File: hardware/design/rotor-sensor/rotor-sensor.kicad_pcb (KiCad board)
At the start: 2 copper layers, 42 x 34.7 mm, 88 parts, among them J2 Conn_01x06, J4 Conn_ARM_JTAG_SWD_10, U1 MCP2021A-500E/SN, U2 AP22804AW5, U4 AP2127K-ADJTRG1, U5 AP22804AW5, U6 ATSAMD21E18A-A, Y1 ABS07-32.768KHZ-7-T

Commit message: Finalizing hardware design
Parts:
- added FID1: Fiducial, Fiducial:Fiducial_0.5mm_Mask1mm, F.Cu at (123.9, 82.4)
- added FID2: Fiducial, Fiducial:Fiducial_0.5mm_Mask1mm, F.Cu at (90.4, 58.3)
- added R21: 10k, Resistor_SMD:R_0402_1005Metric, F.Cu at (98.0, 75.2)
- added R22: 10k, Resistor_SMD:R_0402_1005Metric, B.Cu at (103.2, 75.1)
- moved C14 89.5 mm to (105.5, 51.0)
- moved C24 89.5 mm to (103.2, 72.8)
- moved C9 89.5 mm to (93.0, 55.5)
- moved D2 89.5 mm to (85.4, 73.3)
- moved J2 89.5 mm to (115.1, 78.9)
- moved J4 89.5 mm to (104.0, 53.1)
- moved R1 89.5 mm to (101.9, 68.1)
- moved R20 89.5 mm to (104.3, 68.1)
- moved TP10 89.5 mm to (88.5, 75.9)
- moved TP13 89.5 mm to (85.0, 62.5)
- moved TP16 89.5 mm to (93.0, 70.0)
- moved TP19 89.5 mm to (97.6, 52.0)
- moved TP2 89.5 mm to (93.8, 76.9)
- moved TP3 89.5 mm to (123.6, 76.9)
- moved TP6 89.5 mm to (98.4, 81.5)
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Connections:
- net /M04_EN1/~{SLEEP}/DIAG renamed /M04_~{SLEEP}/DIAG/EN1
- net /M04_INPUT1 renamed /M04_INPUT1/~{ERR}/INPUT1
- net /M04_INPUT1_DIAG renamed /M04_INPUT1_DIAG/OE/~{FLAG}
- net /M04_INPUT2 renamed /M04_INPUT2/INPUT2/INPUT2
- net /M04_INPUT2_DIAG/INPUT2 renamed /M04_INPUT2_DIAG/INPUT1/~{FLAG}
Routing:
- net +BATT: track 36.1 -> 61.8 mm
- net Net-(U2-~{FLG}): track 1.91 -> 12.6 mm
- net /M07_IN1_IN: track 30.6 -> 23.0 mm
- net GND: track 15.7 -> 21.1 mm, vias 41 -> 90
- net +5V: track 43.6 -> 48.2 mm
- net /M07_IN2_IN: track 36.8 -> 32.7 mm, vias 1 -> 2
- net Net-(U5-~{FLG}): track 1.59 -> 4.28 mm, vias 0 -> 1
- net /M07_IN2_VSUP: track 23.4 -> 25.5 mm, vias 1 -> 3
- net /M04_INPUT2/INPUT2/INPUT2: track 34.0 -> 34.9 mm
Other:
- outline, holes or cut-outs redrawn

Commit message: Fab. layer cleanup
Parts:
- U3: value ~ -> BMI088

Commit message: Hardware design finalization
FIxing architecture diagram
Changes to PCB fab layer
Fixes DNF components in schematic
Increases document width
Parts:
- R1, R7: value 10k -> 4.7k
- R18, R19, R2, R3: value 1k -> 0
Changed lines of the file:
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@@
         (effects (font (size 1 1) (thickness 0.15)))
     )
-    (fp_text value "10k" (at 0.471752 -9.121 90) (layer "F.Fab") hide
+    (fp_text value "4.7k" (at 0.471752 -9.121 90) (layer "F.Fab") hide
         (effects (font (size 1 1) (thickness 0.15)))
     )
@@
         (effects (font (size 1 1) (thickness 0.15)))
     )
-    (fp_text value "10k" (at 0 1.17 90) (layer "F.Fab") hide
+    (fp_text value "4.7k" (at 0 1.17 90) (layer "F.Fab") hide
         (effects (font (size 1 1) (thickness 0.15)))
     )
@@
         (effects (font (size 1 1) (thickness 0.15)) (justify mirror))
     )
-    (fp_text value "1k" (at 0 -1.17) (layer "B.Fab")
+    (fp_text value "0" (at 0 -1.17) (layer "B.Fab")
         (effects (font (size 1 1) (thickness 0.15)) (justify mirror))
     )
@@
         (effects (font (size 1 1) (thickness 0.15)) (justify mirror))
     )
-    (fp_text value "1k" (at 0 1.351) (layer "B.Fab")
+    (fp_text value "0" (at 0 1.351) (layer "B.Fab")
         (effects (font (size 1 1) (thickness 0.15)) (justify mirror))
     )
@@
         (effects (font (size 1 1) (thickness 0.15)) (justify mirror))
     )
-    (fp_text value "1k" (at 0 1.351) (layer "B.Fab")
+    (fp_text value "0" (at 0 1.351) (layer "B.Fab")
         (effects (font (size 1 1) (thickness 0.15)) (justify mirror))
     )
@@
         (effects (font (size 1 1) (thickness 0.15)) (justify mirror))
     )
-    (fp_text value "1k" (at 0 -1.17) (layer "B.Fab")
+    (fp_text value "0" (at 0 -1.17) (layer "B.Fab")
         (effects (font (size 1 1) (thickness 0.15)) (justify mirror))
     )

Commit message: Hardware Gen2 design freeze (#14)
* Fix label in connector schematic and added JWPF 3 pin connector
* Optical sensor adapter & CI workflow changes
* 5V rail renamed to VCC
* Fixed size information on some resistors
* Added Hall sensor position on PCB
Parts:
- R18, R19, R2, R3: value 0 -> 1k
- U1: value MCP2021A-500E/SN -> MCP2021A-xxxE/SN
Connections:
- net +5V renamed VCC

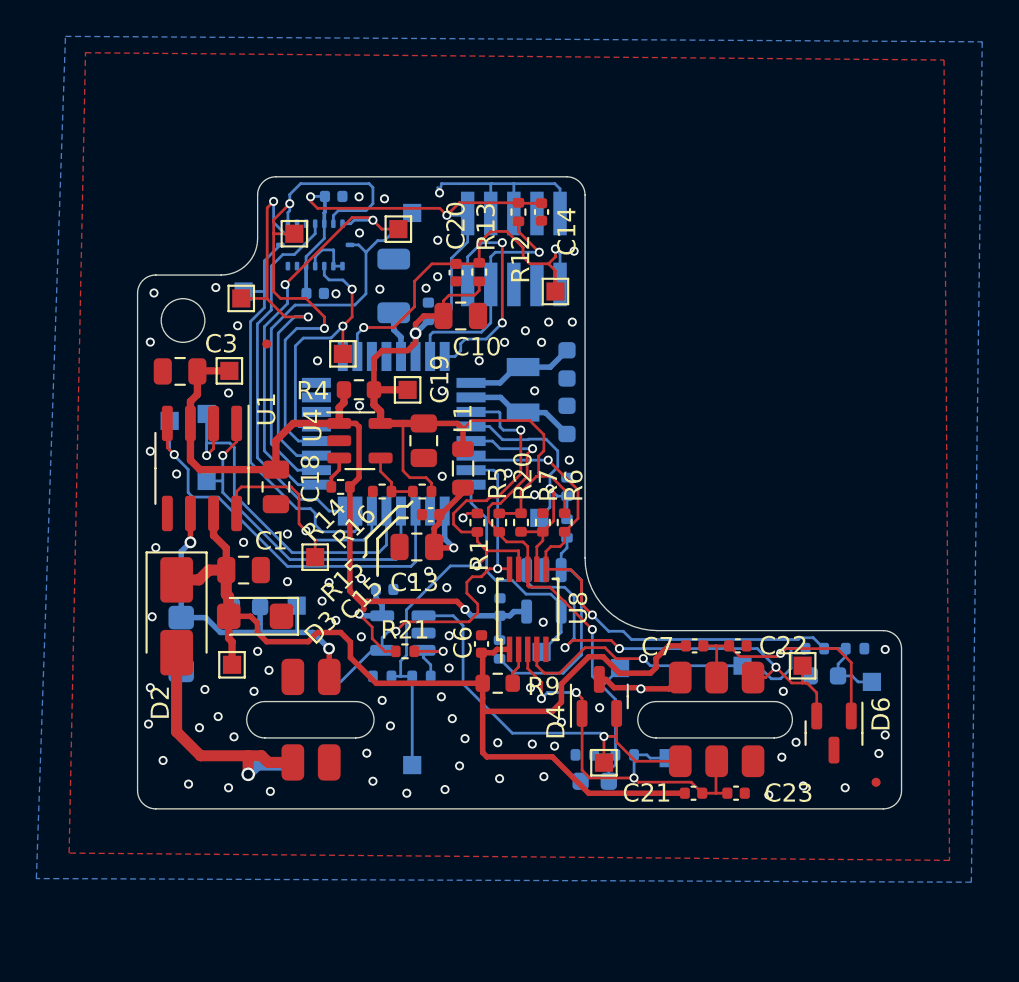
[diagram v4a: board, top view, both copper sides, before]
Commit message: Gen2.1 final hardware design (#16)
* New schematic done

Works with TLIN1028-Q1 transceiver
Added BMP581 pressure sensor
Removed 3wire output stage

* FInal ordered hardware

New 3pin connector
Extra 2pin connector for cadence measurement
No 3pin sensor variant
DC/DC converter for MCU
Pressure sensor
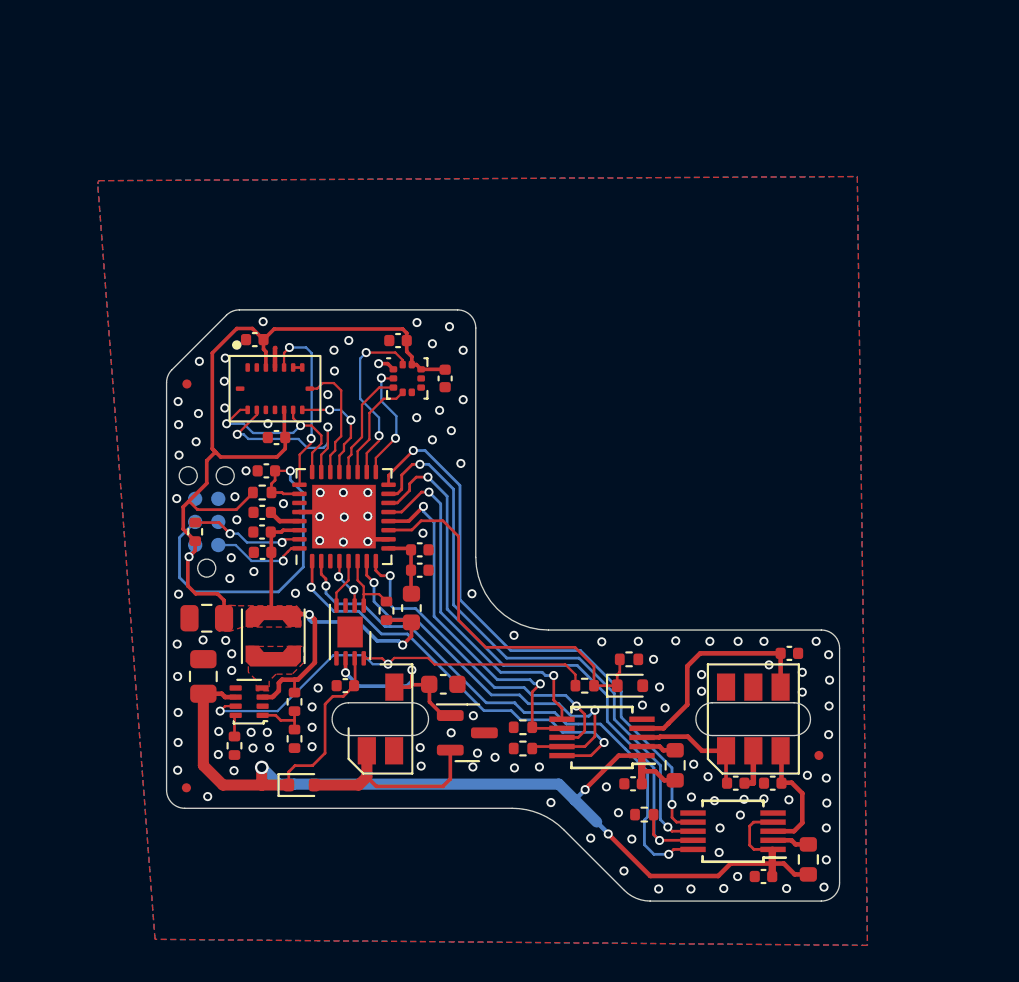
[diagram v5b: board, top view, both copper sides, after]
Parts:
- removed C13, C18, C19: 10u, Capacitor_SMD:C_0805_2012Metric
- removed C14, C21, C22, C24: 220n, Capacitor_SMD:C_0402_1005Metric
- removed C17: 1u, Capacitor_SMD:C_1206_3216Metric
- removed C25: 22n, Capacitor_SMD:C_0603_1608Metric
- removed D3: SMF33CA-DIO, Diode_SMD:D_SMF
- removed D6: PESD5V0S2BT, Package_TO_SOT_SMD:SOT-23
- removed FID2: Fiducial, Fiducial:Fiducial_0.5mm_Mask1mm
- removed J4: Conn_ARM_JTAG_SWD_10, Connector_PinHeader_1.27mm:PinHeader_2x05_P1.27mm_Vertical_SMD
- removed R10, R11, R19, R8: 1k, Resistor_SMD:R_0402_1005Metric
- removed R14, R20, R21, R22: 10k, Resistor_SMD:R_0402_1005Metric
- removed R16: 1.5k, Resistor_SMD:R_0402_1005Metric
- removed TP1: O5, TestPoint:TestPoint_Pad_1.0x1.0mm
- removed TP10: V2, TestPoint:TestPoint_Pad_1.0x1.0mm
- removed TP11: V1, TestPoint:TestPoint_Pad_1.0x1.0mm
- removed TP12: B1, TestPoint:TestPoint_Pad_1.0x1.0mm
- removed TP13: B2, TestPoint:TestPoint_Pad_1.0x1.0mm
- removed TP14: B3, TestPoint:TestPoint_Pad_1.0x1.0mm
- removed TP15: B4, TestPoint:TestPoint_Pad_1.0x1.0mm
- removed TP16: B5, TestPoint:TestPoint_Pad_1.0x1.0mm
- removed TP17: S1, TestPoint:TestPoint_Pad_1.0x1.0mm
- removed TP19: S3, TestPoint:TestPoint_Pad_1.0x1.0mm
- removed TP2: O6, TestPoint:TestPoint_Pad_1.0x1.0mm
- removed TP20: S4, TestPoint:TestPoint_Pad_1.0x1.0mm
- removed TP21: S5, TestPoint:TestPoint_Pad_1.0x1.0mm
- removed TP22: S6, TestPoint:TestPoint_Pad_1.0x1.0mm
- removed TP23: S7, TestPoint:TestPoint_Pad_1.0x1.0mm
- removed TP27: M1, TestPoint:TestPoint_Pad_1.0x1.0mm
- removed TP28: O4, TestPoint:TestPoint_Pad_1.0x1.0mm
- removed TP29: O2, TestPoint:TestPoint_Pad_1.0x1.0mm
- removed TP3: O7, TestPoint:TestPoint_Pad_1.0x1.0mm
- removed TP30: O1, TestPoint:TestPoint_Pad_1.0x1.0mm
- removed TP4: O8, TestPoint:TestPoint_Pad_1.0x1.0mm
- removed TP5: O9, TestPoint:TestPoint_Pad_1.0x1.0mm
- removed TP6: O10, TestPoint:TestPoint_Pad_1.0x1.0mm
- removed TP7: O3, TestPoint:TestPoint_Pad_1.0x1.0mm
- removed TP8: P1, TestPoint:TestPoint_Pad_1.0x1.0mm
- removed TP9: P2, TestPoint:TestPoint_Pad_1.0x1.0mm
- removed U4: AP2127K-ADJTRG1, Package_TO_SOT_SMD:SOT-23-5
- removed U5: AP22804AW5, Package_TO_SOT_SMD:SOT-23-5
- removed Y1: ABS07-32.768KHZ-7-T, Crystal:Crystal_SMD_3215-2Pin_3.2x1.5mm
- added C27: 100n, Capacitor_SMD:C_0402_1005Metric, F.Cu at (119.1, 75.3)
- added C600: 100n, Capacitor_SMD:C_0402_1005Metric, F.Cu at (97.6, 58.1)
- added C601: 100n, Capacitor_SMD:C_0402_1005Metric, F.Cu at (100.2, 60.2)
- added FID3: Fiducial, Fiducial:Fiducial_0.5mm_Mask1mm, F.Cu at (86.0, 60.5)
- added FID4: Fiducial, Fiducial:Fiducial_0.5mm_Mask1mm, F.Cu at (120.7, 80.9)
- added J1: Conn_ARM_SWD_TagConnect_TC2030-NL, Connector:Tag-Connect_TC2030-IDC-NL_2x03_P1.27mm_Vertical, B.Cu at (87.1, 68.1)
- added L3: 2.2u, Inductor_SMD:L_Coilcraft_LPS3010, F.Cu at (90.7, 74.4)
- added U10: ATSAMD21E18A-MUT, Package_DFN_QFN:VQFN-32-1EP_5x5mm_P0.5mm_EP3.5x3.5mm, F.Cu at (94.6, 67.8)
- added U600: BMP581, local_footprints:Bosch_LGA10, F.Cu at (98.1, 60.2)
- C1, C3: value 10u -> 100n; footprint Capacitor_SMD:C_0805_2012Metric -> Capacitor_SMD:C_0402_1005Metric
- C10: value 10u -> 220p; footprint Capacitor_SMD:C_0805_2012Metric -> Capacitor_SMD:C_0603_1608Metric
- C11: value 6.8p -> 22u; footprint Capacitor_SMD:C_0603_1608Metric -> Capacitor_SMD:C_0805_2012Metric; moved to F.Cu
- C12, C8, C9: value 220n -> 100n; moved to F.Cu
- C15, C20, C23, C6: value 220n -> 100n
- C16: value 6.8p -> 10u; footprint Capacitor_SMD:C_0603_1608Metric -> Capacitor_SMD:C_0805_2012Metric; moved to F.Cu
- C2: value 220p -> 100n; footprint Capacitor_SMD:C_0603_1608Metric -> Capacitor_SMD:C_0402_1005Metric; moved to F.Cu
- C4: value 22n -> 10u; footprint Capacitor_SMD:C_0603_1608Metric -> Capacitor_SMD:C_0402_1005Metric; moved to F.Cu
- C5: value 220n -> 10u; moved to F.Cu
- C7: value 220n -> 2.2u
- D1: value SMF33CA-DIO -> BAS3005B02; footprint Diode_SMD:D_SMF -> Diode_SMD:D_SOD-523; moved to F.Cu
- D2: value B140-13-F -> MM5Z3V6T1G; footprint Diode_SMD:D_SMA -> Diode_SMD:D_SOD-523
- D4: value PESD5V0S2BT -> SDT23C15L02
- J2: footprint local_footprints:SMD_6PIN -> local_footprints:SOIC-6
- L1: footprint Inductor_SMD:L_0805_2012Metric -> Inductor_SMD:L_0603_1608Metric
- R17, R3: value 1k -> 4.7k; moved to F.Cu
- R18: value 1k -> 63.4k; footprint Resistor_SMD:R_0402_1005Metric -> Resistor_SMD:R_0603_1608Metric; moved to F.Cu
- R2: value 1k -> 47k; moved to F.Cu
- R4: value 0 -> 4.7k; footprint Resistor_SMD:R_0603_1608Metric -> Resistor_SMD:R_0402_1005Metric
- R5: value 10k -> 20k
- R6: value 10k -> 4.7k
- R7: value 4.7k -> 0
- U1: value MCP2021A-xxxE/SN -> MAX9621AUB+T; footprint Package_SO:SOIC-8_3.9x4.9mm_P1.27mm -> Package_SO:MSOP-10_3x3mm_P0.5mm
- U2: value AP22804AW5 -> MCP2003BT-E/MC; footprint Package_TO_SOT_SMD:SOT-23-5 -> Package_DFN_QFN:DFN-8-1EP_3x2mm_P0.5mm_EP1.7x1.4mm; moved to F.Cu
- U3: moved to F.Cu
- U6: value ATSAMD21E18A-A -> TPS629210DRLR; footprint Package_QFP:TQFP-32_7x7mm_P0.8mm -> Package_TO_SOT_SMD:SOT-583-8; moved to F.Cu
- U7: footprint local_footprints:SMD_4PIN -> local_footprints:SOIC-4
- U8: value ~ -> MAX9621AUB+T
- moved C3 38.0 mm to (116.2, 82.4)
- moved FID1 37.9 mm to (86.0, 82.7)
- moved C4 31.6 mm to (90.1, 69.8)
- moved U1 26.5 mm to (108.8, 79.9), turned to 180 degrees
- moved C16 26.3 mm to (86.9, 76.6)
- moved D2 25.2 mm to (110.3, 77.1), turned to 0 degrees
- moved R12 25.0 mm to (86.4, 68.6), turned to 90 degrees
- moved C7 24.9 mm to (90.1, 67.6), turned to 0 degrees
- moved C1 24.4 mm to (110.5, 82.5), turned to 0 degrees
- moved C11 22.6 mm to (87.1, 73.4), turned to 180 degrees
- moved R7 20.9 mm to (88.6, 80.4)
- moved C10 20.3 mm to (100.1, 77.0), turned to 0 degrees
- moved C6 20.1 mm to (117.7, 87.6), turned to 0 degrees
- moved R9 19.6 mm to (120.1, 86.6), turned to 90 degrees
- moved R6 19.0 mm to (91.9, 80.0), turned to -90 degrees
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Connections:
- C10 pad 1: GND -> /M03_LINE
- C10 pad 2: +3.3V -> GND
- C11 pad 1: /M05_XOUT32 -> +3.3V
- C16 pad 1: /M05_XIN32 -> GND
- C16 pad 2: GND -> +BATT
- C2 pad 1: Net-(D1-A2) -> GND
- C2 pad 2: GND -> +BATT
- C23 pad 2: /M07_IN1_IN -> /M04_IN3_IN
- C3 pad 1: VCC -> GND
- C3 pad 2: GND -> /M04_IN1_IN
- C4 pad 2: /M04_INPUT2/INPUT2/INPUT2 -> +3.3V
- C5 pad 2: VCC -> /VDDANA
- C7 pad 1: /M07_IN2_IN -> GND
- C7 pad 2: +BATT -> /VDDCORE
- D1 pad 1: GND -> +BATT
- D1 pad 2: Net-(D1-A2) -> VS
- D2 pad 1: +BATT -> /M03_VMON
- D2 pad 2: Net-(D2-A) -> GND
- D4 pad 1: /M07_IN1_IN -> /M03_LINE
- D4 pad 2: /M07_IN1_VSUP -> VS
- J2 pad 1: GND -> /M04_IN1_IN
- J2 pad 2: /M07_IN2_IN -> GND
- J2 pad 3: /M07_IN2_VSUP -> /M04_IN3_IN
- J2 pad 4: /M07_IN1_VSUP -> /M04_IN2_IN
- J2 pad 5: /M07_IN1_IN -> GND
- R1 pad 2: /M04_INPUT1_DIAG/OE/~{FLAG} -> /M04_INPUT3_DIAG/OE
- R15 pad 1: Net-(U4-ADJ) -> GND
- R15 pad 2: +3.3V -> /M04_INPUT2_DIAG/INPUT1
- R17 pad 2: /M04_INPUT1_DIAG/OE/~{FLAG} -> /M04_INPUT1_DIAG/OE
- R18 pad 1: GND -> +BATT
- R18 pad 2: /M04_INPUT1/~{ERR}/INPUT1 -> Net-(U1-ISET)
- R2 pad 1: /M04_INPUT2/INPUT2/INPUT2 -> /M03_REGEN
- R2 pad 2: /M07_IN2_IN -> /M03_VMON
- R3 pad 1: GND -> /M03_VMON
- R3 pad 2: /M04_INPUT2/INPUT2/INPUT2 -> GND
- R4 pad 2: VCC -> /M03_RXD
- R5 pad 1: /M04_INPUT1/~{ERR}/INPUT1 -> +3.3V
- R5 pad 2: +3.3V -> /TPS629210_FB
- R6 pad 1: /M04_INPUT2/INPUT2/INPUT2 -> /TPS629210_FB
- R6 pad 2: +3.3V -> GND
- R7 pad 1: GND -> /TPS629210_MODE
- R7 pad 2: /M04_INPUT2_DIAG/INPUT1/~{FLAG} -> GND
- U1 pad 1: /M02_RXD -> +BATT
- U1 pad 2: /M02_CS -> Net-(U1-ISET)
- U1 pad 3: VCC -> /M04_IN1_IN
- U1 pad 4: /M02_TXD -> /M04_IN2_IN
- U1 pad 6: Net-(D1-A2) -> /M04_INPUT2/INPUT2
- U1 pad 7: +BATT -> /M04_INPUT2_DIAG/INPUT1
- U1 pad 8: /M02_TXE -> /M04_INPUT1/~{ERR}
- U2 pad 1: /M07_IN2_VSUP -> /M03_RXD
- U2 pad 2: GND -> /M03_EN
- U2 pad 3: Net-(U2-~{FLG}) -> unconnected-(U2-~{WAKE}-Pad3)
- U2 pad 4: /M04_EN2 -> /M03_TXD
- U2 pad 5: VCC -> GND
- U3 pad 10: /M06_SDO -> /M06_BMI088_MISO
- U3 pad 12: /M06_GYRO_INT -> unconnected-(U3-INT3-Pad12)
- U3 pad 14: /M06_CS_ACCEL -> /M06_BMI088_CSA
- U3 pad 15: /M06_SDO -> /M06_BMI088_MISO
- U3 pad 16: /M06_ACCEL_INT -> unconnected-(U3-INT1-Pad16)
- U3 pad 5: /M06_CS_GYRO -> /M06_BMI088_CSG
- U3 pad 8: /M06_SCK -> /M05_BMI088_SCK
- U3 pad 9: /M06_SDI -> /M05_BMI088_MOSI
- U6 pad 1: /M05_XIN32 -> /TPS629210_FB
- U6 pad 2: /M05_XOUT32 -> unconnected-(U6-PG-Pad2)
- U6 pad 3: /M04_INPUT1_DIAG/OE/~{FLAG} -> +3.3V
- U6 pad 4: /M04_INPUT2_DIAG/INPUT1/~{FLAG} -> /TPS629210_SW
- U6 pad 5: /M04_INPUT1/~{ERR}/INPUT1 -> GND
- U6 pad 6: /M04_INPUT2/INPUT2/INPUT2 -> +BATT
- U6 pad 7: /M04_~{SLEEP}/DIAG/EN1 -> /M03_REGEN
- U6 pad 8: /M04_EN2 -> /TPS629210_MODE
- U7 pad 1: Net-(D2-A) -> VS
- U7 pad 2: unconnected-(U7-Pad2) -> GND
- U7 pad 3: Net-(D1-A2) -> /M03_LINE
- U8 pad 10: /M04_~{SLEEP}/DIAG/EN1 -> /M04_~{SLEEP2}/DIAG2
- U8 pad 3: /M07_IN1_IN -> /M04_IN3_IN
- U8 pad 4: /M07_IN2_IN -> +BATT
- U8 pad 6: /M04_INPUT2/INPUT2/INPUT2 -> unconnected-(U8-DOUT2-Pad6)
- U8 pad 7: /M04_INPUT2_DIAG/INPUT1/~{FLAG} -> /M04_NC/INPUT3
- U8 pad 8: /M04_INPUT1/~{ERR}/INPUT1 -> /M04_INPUT3/~{ERR}
- U8 pad 9: /M04_INPUT1_DIAG/OE/~{FLAG} -> /M04_INPUT3_DIAG/OE
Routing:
- net VCC: track 48.2 -> 0.00 mm, vias 2 -> 0
- net /M04_INPUT2/INPUT2/INPUT2: track 34.9 -> 0.00 mm, vias 2 -> 0
- net /M04_INPUT3_DIAG/OE: track 0.00 -> 34.0 mm, vias 0 -> 2
- net /M07_IN2_IN: track 32.7 -> 0.00 mm, vias 2 -> 0
- net /M04_INPUT3/~{ERR}: track 0.00 -> 32.5 mm, vias 0 -> 2
- net /M04_INPUT1_DIAG/OE/~{FLAG}: track 32.4 -> 0.00 mm, vias 2 -> 0
- net /M04_NC/INPUT3: track 0.00 -> 32.4 mm, vias 0 -> 2
- net /M04_~{SLEEP2}/DIAG2: track 0.00 -> 30.7 mm, vias 0 -> 2
- net /M06_SDO: track 30.0 -> 0.00 mm, vias 2 -> 0
- net /M04_INPUT1/~{ERR}/INPUT1: track 29.9 -> 0.00 mm, vias 2 -> 0
- net /M07_IN2_VSUP: track 25.5 -> 0.00 mm, vias 3 -> 0
- net /M03_REGEN: track 0.00 -> 24.6 mm, vias 0 -> 2
- net /M04_~{SLEEP1}/DIAG1: track 0.00 -> 23.8 mm, vias 0 -> 2
- net /M02_TXD: track 23.3 -> 0.00 mm, vias 1 -> 0
- net /M06_CS_ACCEL: track 23.2 -> 0.00 mm, vias 2 -> 0
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- added copper zone on F.Cu, net +3.3V
- added copper zone on F.Cu, net /TPS629210_SW
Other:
- board size 42 x 34.7 mm -> 37 x 32.5 mm
